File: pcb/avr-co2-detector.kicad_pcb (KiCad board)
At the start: 2 copper layers, 100 x 70 mm, 70 parts, among them J1 USB TYPE-C, J2 Backlight, J3 Backlight, J4 LCD0802, J5 AVR-ISP-10, J6 BH1.27-6-2, SW1 "Reset", SW2 "Reset", U1 ATtiny2313A-SU, U2 FT232RL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

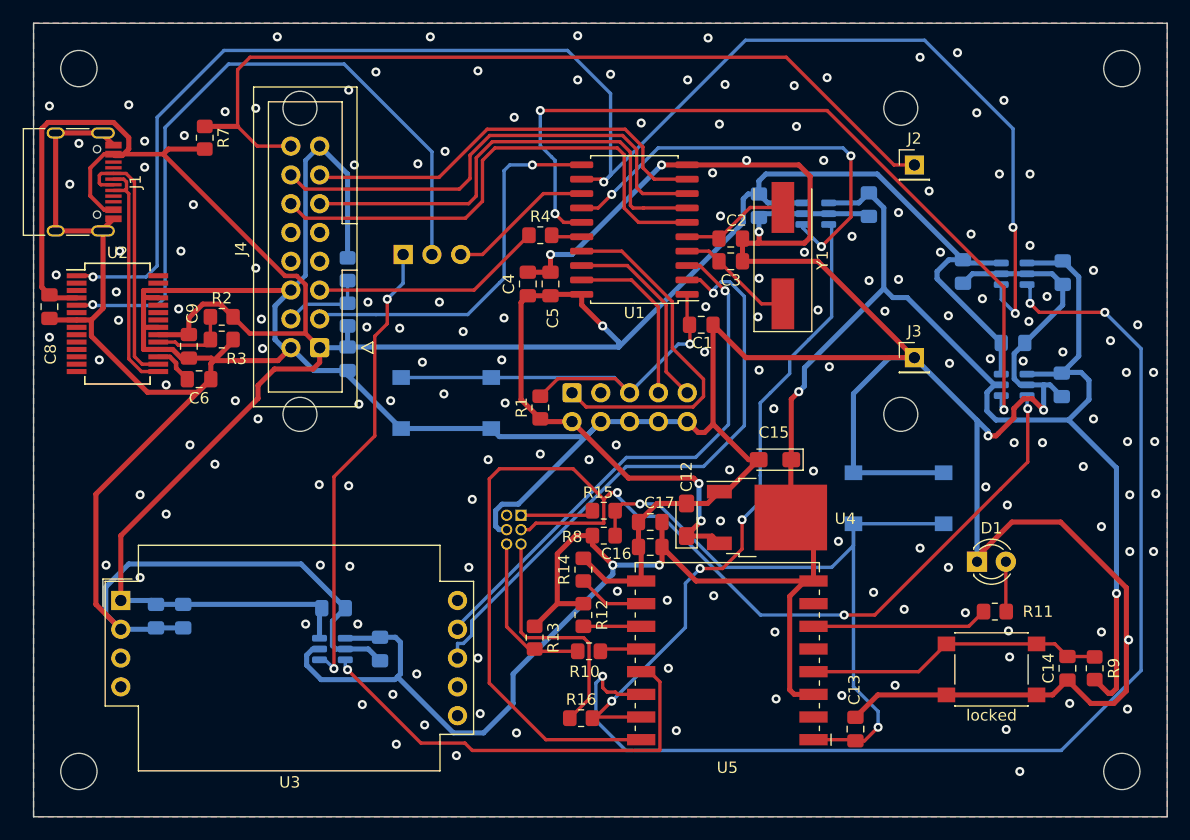
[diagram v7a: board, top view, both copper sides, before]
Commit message: Added PCB description to silkscreen, rounded PCB corners, generated Gerber and drill files
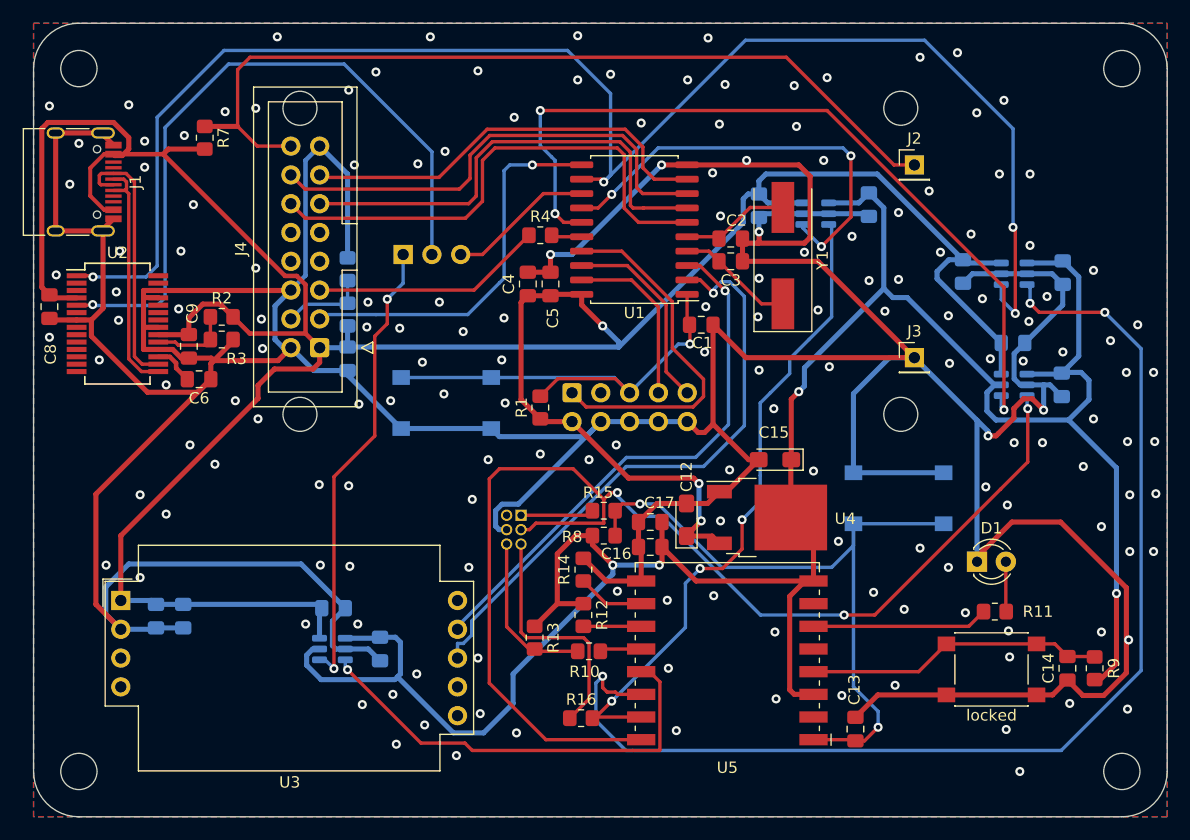
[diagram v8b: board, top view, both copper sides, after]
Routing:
- net +3.3V: track 220.1 -> 217.9 mm
- net GND: track 505.3 -> 503.8 mm
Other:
- outline, holes or cut-outs redrawn
- board text added: "${TITLE} ${REVISION} © ${ISSUE_DATE} ${COMPANY}"
